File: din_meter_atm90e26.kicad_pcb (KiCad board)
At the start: 2 copper layers, 32 x 31.1 mm, 61 parts, among them J1 USEL, J2 MMD1, J3 MMD0, J4 CONN_02X18, J5 CONN_01X10, J6 USEL, J7 MMD1, J8 MMD0, M1 ATM90E26_ATM90E26, M2 ATM90E26_ATM90E26, Y1 Crystal_Small, Y2 Crystal_Small

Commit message: added tapr licence on silk
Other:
- board text added: "Dual ATM90E26 Metering v1.3 22/01/2018 OSHW TAPR"
- board text removed: "Dual ATM90E26 Metering v1.3 22/01/2018"
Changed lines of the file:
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@@
   (page A4)
   (layers
-    (0 F.Cu mixed)
-    (31 B.Cu mixed)
+    (0 F.Cu mixed hide)
+    (31 B.Cu mixed hide)
     (32 B.Adhes user hide)
     (33 F.Adhes user hide)
@@
     (35 F.Paste user hide)
     (36 B.SilkS user)
-    (37 F.SilkS user)
+    (37 F.SilkS user hide)
     (38 B.Mask user)
     (39 F.Mask user hide)
     (40 Dwgs.User user hide)
     (41 Cmts.User user hide)
-    (42 Eco1.User user)
-    (43 Eco2.User user)
+    (42 Eco1.User user hide)
+    (43 Eco2.User user hide)
     (44 Edge.Cuts user)
     (45 Margin user hide)
-    (46 B.CrtYd user)
+    (46 B.CrtYd user hide)
     (47 F.CrtYd user hide)
-    (48 B.Fab user)
-    (49 F.Fab user)
+    (48 B.Fab user hide)
+    (49 F.Fab user hide)
   )
   (setup
@@
     )
   )
-  (gr_text "Dual ATM90E26 Metering v1.3\n22/01/2018" (at 145.402 70.293 270) (layer B.SilkS)
+  (gr_text "Dual ATM90E26 Metering v1.3\n22/01/2018\nOSHW TAPR" (at 145.402 70.293 270) (layer B.SilkS)
     (effects (font (size 0.6 0.6) (thickness 0.15)) (justify mirror))
   )

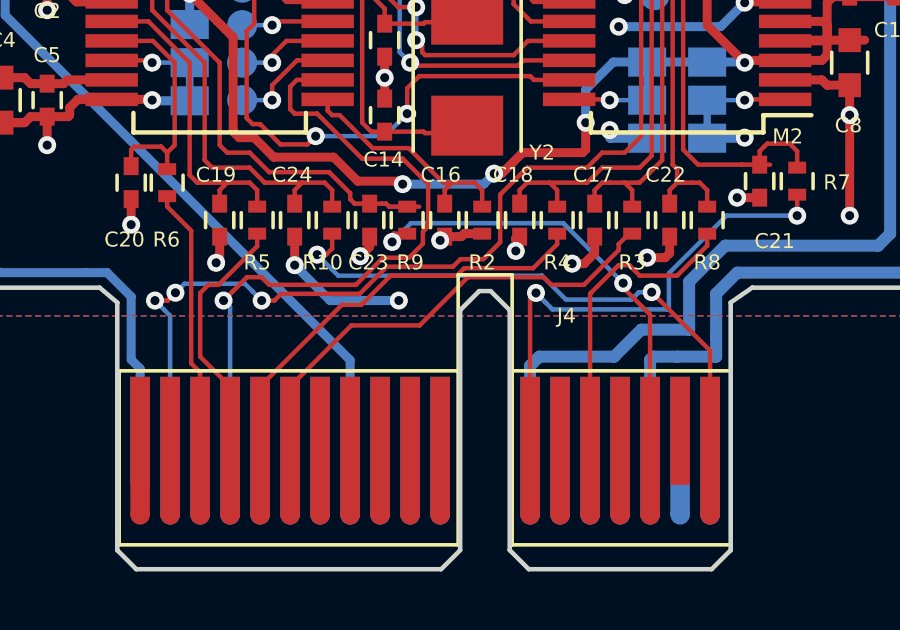
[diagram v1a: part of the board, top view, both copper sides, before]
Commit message: New gerbers with silk and vias on pads fixes
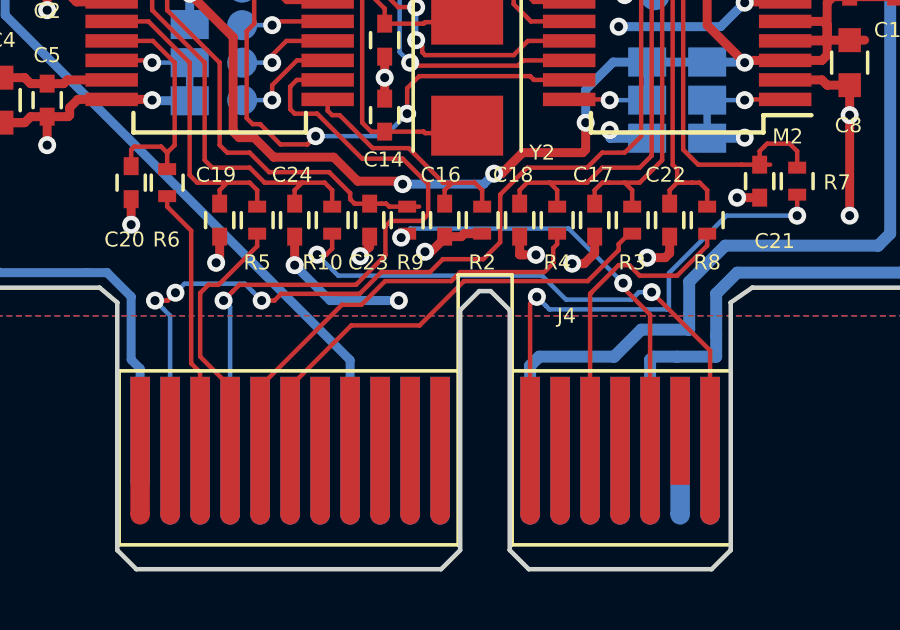
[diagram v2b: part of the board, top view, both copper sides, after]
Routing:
- net GNDD: track 104.9 -> 106.2 mm
- net I2P_1_IN: track 15.3 -> 14.3 mm
